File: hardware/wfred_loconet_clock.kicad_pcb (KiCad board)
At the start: 2 copper layers, 32 x 86.9 mm, 30 parts, among them K201 UART_ESP, P201 ESP_BOOTLOAD, P301 CLOCK, SW301 SW_PUSH, SW302 SW_PUSH, SW303 SW_PUSH, SW304 SW_PUSH, U101 L6920D, U201 ESP-12E

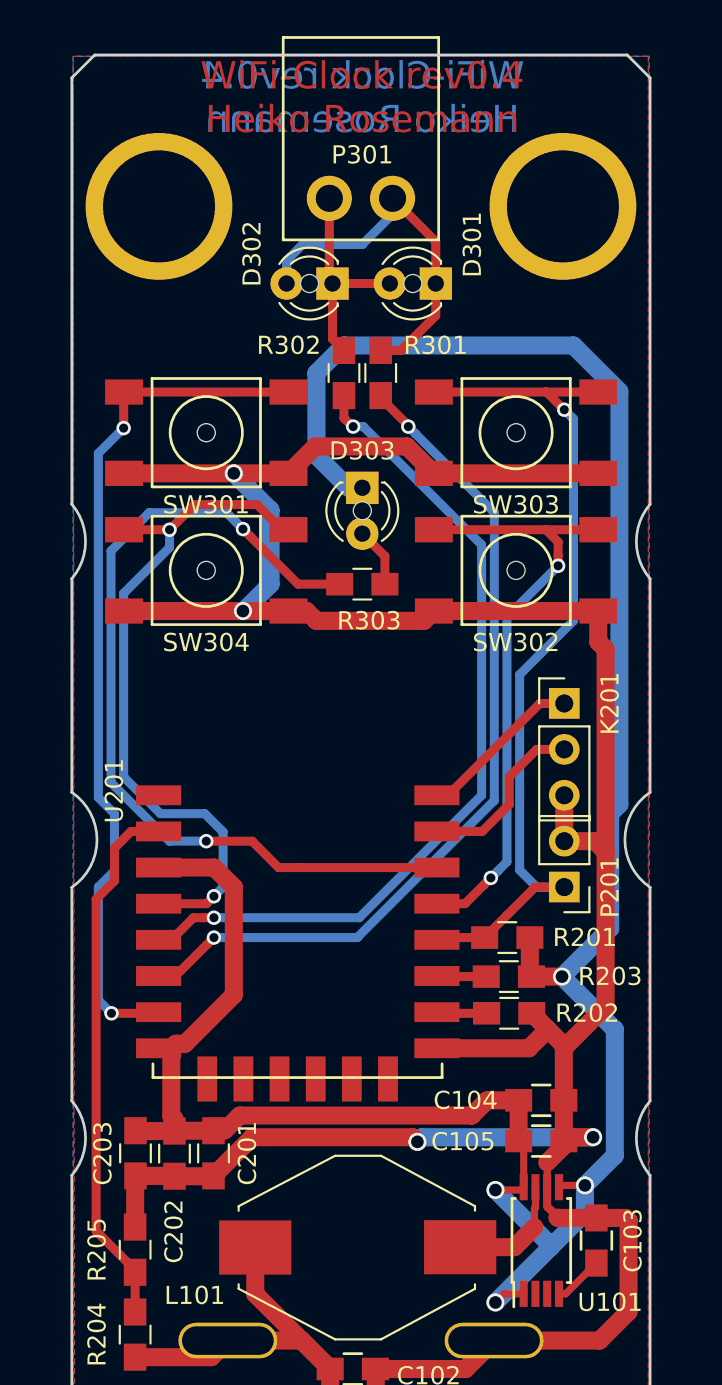
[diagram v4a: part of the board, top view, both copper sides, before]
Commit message: Add second clock output...
...while removing (so far) unused key
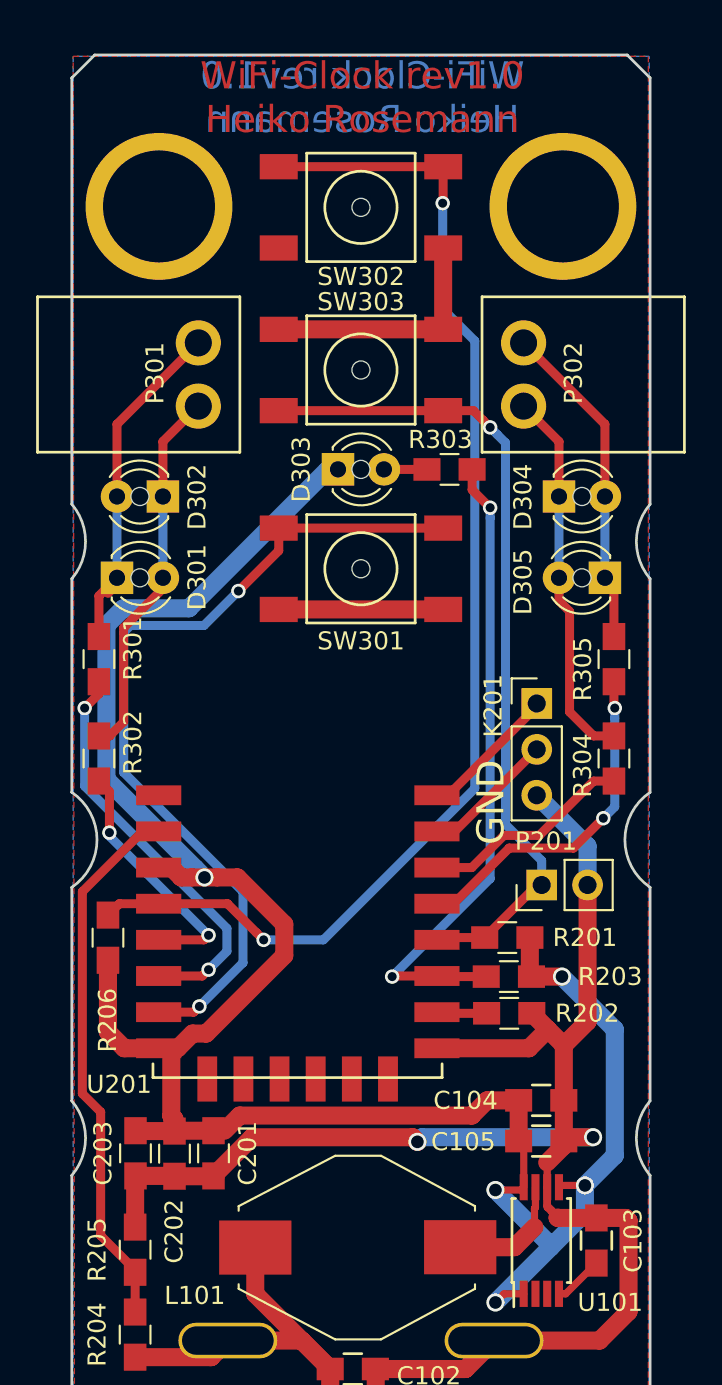
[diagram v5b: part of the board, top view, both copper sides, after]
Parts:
- removed SW304: SW_PUSH, myFootprints:Taster_9319
- added D304: red, myFootprints:LED_D3.0mm, F.Cu at (111.0, 81.0)
- added D305: red, myFootprints:LED_D3.0mm, F.Cu at (113.5, 85.5)
- added P302: CLOCK2, myFootprints:AKL183-02, F.Cu at (109.0, 76.0)
- added R206: 10k, Capacitors_SMD:C_0805_HandSoldering, F.Cu at (86.0, 105.4)
- added R304: 220, Capacitors_SMD:C_0805_HandSoldering, F.Cu at (114.0, 95.5)
- added R305: 220, Capacitors_SMD:C_0805_HandSoldering, F.Cu at (114.0, 90.0)
- D303: value red -> green
- P301: value CLOCK -> CLOCK1
- moved R302 25.3 mm to (85.5, 95.5)
- moved D301 24.0 mm to (86.5, 85.5), turned to 0 degrees
- moved R301 22.2 mm to (85.5, 90.0)
- moved SW302 21.8 mm to (100.0, 65.0)
- moved D302 15.1 mm to (89.0, 81.0)
- moved P301 13.4 mm to (91.0, 72.5), turned to 270 degrees
- moved SW301 11.4 mm to (100.0, 85.0)
- moved SW303 9.26 mm to (100.0, 74.0), turned to 180 degrees
- moved R303 7.98 mm to (104.9, 79.5), turned to 180 degrees
- moved D303 1.69 mm to (98.7, 79.5), turned to 0 degrees
- moved K201 1.52 mm to (109.7, 92.5)
- moved P201 1.26 mm to (110.0, 102.5), turned to 90 degrees
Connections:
- R203 pad 1: Net-(R203-Pad1) -> STATUS_LED
- U201 pad 11: Net-(R203-Pad1) -> STATUS_LED
- U201 pad 13: KEY_HOUR -> CLOCK4
- U201 pad 14: STATUS_LED -> CLOCK3
- U201 pad 4: KEY -> KEY_HOUR
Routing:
- net GND: track 173.0 -> 117.6 mm, vias 4 -> 2
- net KEY: track 38.1 -> 0.00 mm, vias 2 -> 0
- net KEY_HOUR: track 34.5 -> 69.2 mm
- net CLOCK2: track 46.1 -> 13.2 mm
- net CLOCK1: track 46.9 -> 22.4 mm
- net Net-(D304-Pad1): track 0.00 -> 21.0 mm
- net CLOCK4: track 0.00 -> 19.7 mm, vias 0 -> 2
- net Net-(D304-Pad2): track 0.00 -> 18.3 mm
- net VCC: track 152.1 -> 135.7 mm, vias 4 -> 5
- net CLOCK3: track 0.00 -> 12.5 mm
- net STATUS_LED: track 47.3 -> 36.0 mm
- net Net-(D301-Pad2): track 11.9 -> 21.0 mm
- net Net-(R203-Pad1): track 3.44 -> 0.00 mm
- net KEY_MINUTE: track 49.3 -> 45.9 mm
- net Net-(K201-Pad2): track 10.5 -> 8.10 mm
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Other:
- board text added: "GND"
- board text added: "WiFi-Clock rev1.0 Heiko Rosemann"
- board text removed: "WiFi-Clock rev0.4 Heiko Rosemann"

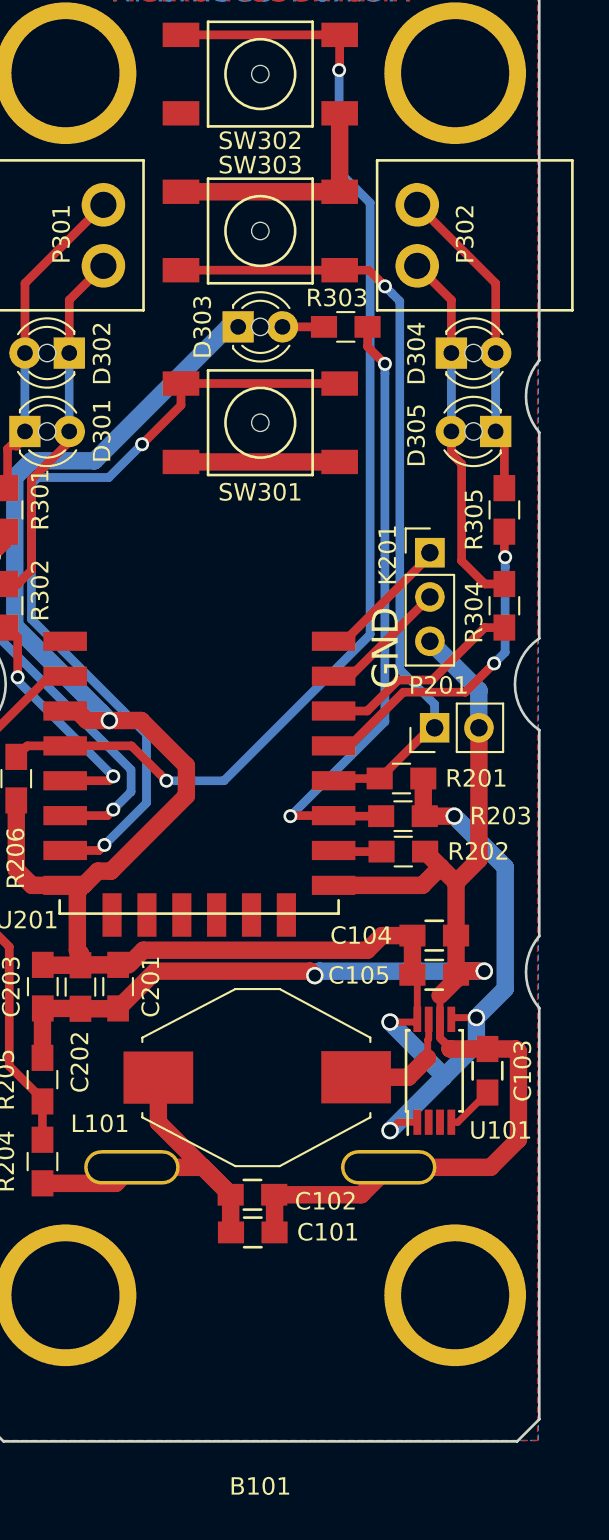
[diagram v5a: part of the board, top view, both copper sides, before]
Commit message: Fixed missing GND connection on PCB...
...found during order process.
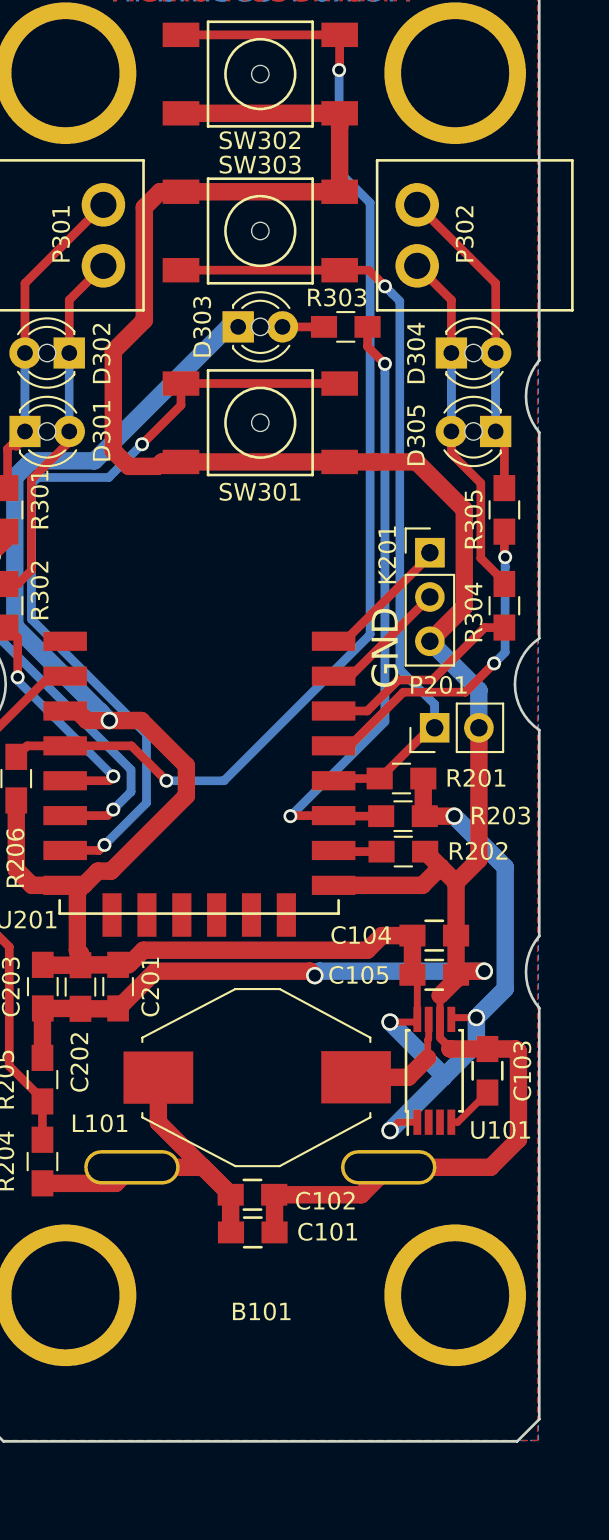
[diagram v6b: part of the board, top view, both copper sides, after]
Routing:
- net GND: track 117.6 -> 165.7 mm
- net Net-(D304-Pad1): track 21.0 -> 20.3 mm
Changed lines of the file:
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@@
   (general
     (links 72)
-    (no_connects 1)
-    (area 67.426099 56.290999 191.967001 147.0998)
+    (no_connects 0)
+    (area 67.426099 56.290999 191.967001 145.5758)
     (thickness 1.6)
     (drawings 19338)
-    (tracks 265)
+    (tracks 281)
     (zones 0)
     (modules 35)
@@
     (visible_elements FFFECE79)
     (pcbplotparams
-      (layerselection 0x00030_80000001)
-      (usegerberextensions false)
+      (layerselection 0x010f0_80000001)
+      (usegerberextensions true)
       (excludeedgelayer true)
       (linewidth 0.100000)
@@
       (psa4output false)
       (plotreference true)
-      (plotvalue true)
+      (plotvalue false)
       (plotinvisibletext false)
       (padsonsilk false)
-      (subtractmaskfromsilk false)
+      (subtractmaskfromsilk true)
       (outputformat 1)
       (mirror false)
-      (drillshape 1)
+      (drillshape 0)
       (scaleselection 1)
-      (outputdirectory ""))
+      (outputdirectory ../../../bestellungen/2019-08-04-wiClock-1.0-PCB/))
   )
   (net 0 "")
@@
   (module myFootprints:NEW_AGE_COMPACT_AA_PCBEdges (layer F.Cu)
     (at 100 100 180)
-    (fp_text reference B101 (at 0 -46.0248 180) (layer F.SilkS)
+    (fp_text reference B101 (at -0.076 -36.017 180) (layer F.SilkS)
       (effects (font (size 1 1) (thickness 0.15)))
     )
@@
   (segment (start 92.634 127.7114) (end 96.7234 127.7114) (width 1) (layer F.Cu) (net 1) (status 10))
   (segment (start 96.7234 127.7114) (end 98.298 129.286) (width 1) (layer F.Cu) (net 1) (status 20))
+  (segment (start 95.45 87.25) (end 94.36 87.25) (width 1) (layer F.Cu) (net 2))
+  (segment (start 94.36 87.25) (end 94.107 87.503) (width 1) (layer F.Cu) (net 2))
+  (segment (start 94.107 87.503) (end 92.456 87.503) (width 1) (layer F.Cu) (net 2))
+  (segment (start 94.239 71.75) (end 95.45 71.75) (width 1) (layer F.Cu) (net 2))
+  (segment (start 92.456 87.503) (end 91.567 86.614) (width 1) (layer F.Cu) (net 2))
+  (segment (start 91.567 86.614) (end 91.567 80.899) (width 1) (layer F.Cu) (net 2))
+  (segment (start 91.567 80.899) (end 93.345 79.121) (width 1) (layer F.Cu) (net 2))
+  (segment (start 93.345 79.121) (end 93.345 72.644) (width 1) (layer F.Cu) (net 2))
+  (segment (start 93.345 72.644) (end 94.239 71.75) (width 1) (layer F.Cu) (net 2))
+  (segment (start 108.967 87.25) (end 106.6 87.25) (width 1) (layer F.Cu) (net 2))
+  (segment (start 111.698989 89.981989) (end 108.967 87.25) (width 1) (layer F.Cu) (net 2))
+  (segment (start 111.698989 95.565011) (end 111.698989 89.981989) (width 1) (layer F.Cu) (net 2))
+  (segment (start 109.728 97.536) (end 111.698989 95.565011) (width 1) (layer F.Cu) (net 2))
+  (segment (start 106.6 87.25) (end 104.55 87.25) (width 1) (layer F.Cu) (net 2))
+  (segment (start 95.45 67.25) (end 104.55 67.25) (width 1) (layer F.Cu) (net 2))
+  (segment (start 104.55 67.25) (end 104.55 68.072) (width 1) (layer F.Cu) (net 2))
   (segment (start 109.728 97.536) (end 112.54 100.348) (width 1) (layer B.Cu) (net 2))
   (segment (start 112.54 100.348) (end 112.54 102.5) (width 1) (layer B.Cu) (net 2))
@@
   (segment (start 104.55 62.75) (end 95.45 62.75) (width 0.5) (layer F.Cu) (net 18))
   (segment (start 89.505 103.536) (end 89.536 103.505) (width 0.5) (layer F.Cu) (net 18) (status 30))
+  (segment (start 112.649 92.774) (end 112.649 88.461792) (width 0.5) (layer F.Cu) (net 19))
+  (segment (start 114 94.25) (end 114 94.125) (width 0.5) (layer F.Cu) (net 19))
+  (segment (start 114 94.125) (end 112.649 92.774) (width 0.5) (layer F.Cu) (net 19))
+  (segment (start 112.649 88.461792) (end 110.96 86.772792) (width 0.5) (layer F.Cu) (net 19))
+  (segment (start 110.96 86.772792) (end 110.96 85.5) (width 0.5) (layer F.Cu) (net 19))
   (segment (start 109 76) (end 110.96 77.96) (width 0.5) (layer F.Cu) (net 19))
   (segment (start 110.96 77.96) (end 110.96 81) (width 0.5) (layer F.Cu) (net 19))
   (segment (start 110.96 85.5) (end 110.96 81) (width 0.5) (layer B.Cu) (net 19))
-  (segment (start 114 94.25) (end 112.875 94.25) (width 0.5) (layer F.Cu) (net 19))
-  (segment (start 112.875 94.25) (end 111.544999 92.919999) (width 0.5) (layer F.Cu) (net 19))
-  (segment (start 111.544999 92.919999) (end 111.544999 87.357791) (width 0.5) (layer F.Cu) (net 19))
-  (segment (start 111.544999 87.357791) (end 110.96 86.772792) (width 0.5) (layer F.Cu) (net 19))
-  (segment (start 110.96 86.772792) (end 110.96 85.5) (width 0.5) (layer F.Cu) (net 19))
   (segment (start 109 72.5) (end 113.5 77) (width 0.5) (layer F.Cu) (net 20))
   (segment (start 113.5 77) (end 113.5 81) (width 0.5) (layer F.Cu) (net 20))
